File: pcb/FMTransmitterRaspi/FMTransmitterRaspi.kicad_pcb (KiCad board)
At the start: 2 copper layers, 56.6 x 52.3 mm, 35 parts, among them J1 Antenna/External Power, J2 GPIO, J3 GPIO, J4 USB-C Power, J5 Line In/Out, J6 Line In/Out 2, U1 QN8072, U2 PCM5102A, U3 ME6211C33M5, Y1 24MHz, Y2 12MHz

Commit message: corrected wrong symbol of qn8027, too wide board shape
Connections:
- U1 pad 10: /GPIO3/SCL1 -> Net-(U1-ALI)
- U1 pad 6: Net-(U1-ALI) -> /GPIO3/SCL1
- U1 pad 7: Net-(U1-ARI) -> /GPIO2/SDA1
- U1 pad 9: /GPIO2/SDA1 -> Net-(U1-ARI)
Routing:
- net /GPIO3/SCL1: track 35.6 -> 44.0 mm, vias 0 -> 2
- net Net-(U1-ALI): track 18.2 -> 10.4 mm
- net /GPIO2/SDA1: track 36.9 -> 42.9 mm, vias 0 -> 2
- net Net-(U1-ARI): track 8.46 -> 7.22 mm
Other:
- board size 56.6 x 52.3 mm -> 56.4 x 52.3 mm
- board text added: "Raspi Audio DAC FM Transmitter Bernd Strobel 09/2026 Rev. 1"
- board text removed: "Raspi Audio DAC FM Transmitter Bernd Strobel 09/2026"

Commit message: pcb beautified
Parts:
- C14, C9: value 2u2 -> 470n
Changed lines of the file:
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@@
 		(tags "C Rect series Radial pin pitch 7.50mm length 9mm width 2.7mm Capacitor")
 		(property "Reference" "C18"
-			(at 6.544 2.54 0)
+			(at 7.56 2.54 0)
 			(layer "F.SilkS")
 			(effects
@@
 		)
 		(property "Value" "2.2n"
-			(at 1.464 2.54 0)
+			(at 4.004 2.54 0)
 			(layer "F.SilkS")
 			(effects
@@
 		(at 156.308 130.988 -90)
 		(property "Reference" "J5"
-			(at 5.842 10.588 0)
+			(at -5.842 10.842 0)
 			(unlocked yes)
 			(layer "F.SilkS")
@@
 		)
 		(property "Value" "Line In/Out"
-			(at 5.842 4.746 0)
+			(at -5.842 5 0)
 			(unlocked yes)
 			(layer "F.SilkS")
@@
 		(tags "C Rect series Radial pin pitch 5.00mm length 7.2mm width 6.0mm Capacitor R82")
 		(property "Reference" "C14"
-			(at 7.032 -1.778 180)
+			(at -2.112 -1.524 180)
 			(layer "F.SilkS")
 			(effects
@@
 			)
 		)
-		(property "Value" "2u2"
-			(at 7.032 1.524 180)
+		(property "Value" "470n"
+			(at -2.112 2.032 180)
 			(layer "F.SilkS")
 			(effects
@@
 		(tags "C Rect series Radial pin pitch 5.00mm length 7.2mm width 6.0mm Capacitor R82")
 		(property "Reference" "C9"
-			(at 7.072 -1.016 180)
+			(at 8.596 0.762 180)
 			(layer "F.SilkS")
 			(effects
@@
 			)
 		)
-		(property "Value" "2u2"
-			(at 7.072 1.778 180)
+		(property "Value" "470n"
+			(at 7.072 0.762 180)
 			(layer "F.SilkS")
 			(effects
@@
 	)
 	(segment
-		(start 115.374 105.468)
-		(end 114.224 104.318)
+		(start 135.564 114.983807)
+		(end 135.564 111.921882)
 		(width 0.2)
 		(layer "F.Cu")
-		(net "/GPIO2{slash}SDA1")
+		(net "/GPIO3{slash}SCL1")
 	)
 	(segment
-		(start 117.592778 105.468)
-		(end 117.592778 106.033685)
+		(start 101.778 106.858)
+		(end 103.168 108.248)
 		(width 0.2)
 		(layer "F.Cu")
-		(net "/GPIO2{slash}SDA1")
+		(net "/GPIO3{slash}SCL1")
 	)
 	(segment
-		(start 135.164 113.849094)
-		(end 135.164 112.087568)
+		(start 114.224 106.858)
+		(end 114.789685 106.858)
 		(width 0.2)
 		(layer "F.Cu")
-		(net "/GPIO2{slash}SDA1")
+		(net "/GPIO3{slash}SCL1")
 	)
 	(segment
-		(start 103.168 105.708)
-		(end 112.834 105.708)
+		(start 114.789685 106.858)
+		(end 115.939685 108.008)
 		(width 0.2)
 		(layer "F.Cu")
-		(net "/GPIO2{slash}SDA1")
+		(net "/GPIO3{slash}SCL1")
 	)
 	(segment
-		(start 112.834 105.708)
-		(end 114.224 104.318)
+		(start 135.052754 115.495053)
+		(end 135.564 114.983807)
 		(width 0.2)
 		(layer "F.Cu")
-		(net "/GPIO2{slash}SDA1")
+		(net "/GPIO3{slash}SCL1")
 	)
 	(segment
-		(start 124.044093 112.485)
-		(end 130.731411 112.485)
+		(start 124.213407 113.22)
+		(end 129.911243 113.22)
 		(width 0.2)
 		(layer "F.Cu")
-		(net "/GPIO2{slash}SDA1")
+		(net "/GPIO3{slash}SCL1")
 	)
 	(segment
-		(start 135.164 112.087568)
-		(end 134.514432 111.438)
+		(start 129.911243 113.22)
+		(end 129.934728 113.243485)
 		(width 0.2)
 		(layer "F.Cu")
-		(net "/GPIO2{slash}SDA1")
+		(net "/GPIO3{slash}SCL1")
 	)
 	(segment
-		(start 134.412547 114.600547)
-		(end 135.164 113.849094)
+		(start 119.001407 108.008)
+		(end 124.213407 113.22)
 		(width 0.2)
 		(layer "F.Cu")
-		(net "/GPIO2{slash}SDA1")
+		(net "/GPIO3{slash}SCL1")
 	)
 	(segment
-		(start 134.514432 111.438)
-		(end 133.714 111.438)
+		(start 135.564 111.921882)
+		(end 134.580118 110.938)
 		(width 0.2)
 		(layer "F.Cu")
-		(net "/GPIO2{slash}SDA1")
+		(net "/GPIO3{slash}SCL1")
 	)
 	(segment
-		(start 117.592778 106.033685)
-		(end 124.044093 112.485)
+		(start 112.834 108.248)
+		(end 114.224 106.858)
 		(width 0.2)
 		(layer "F.Cu")
-		(net "/GPIO2{slash}SDA1")
+		(net "/GPIO3{slash}SCL1")
 	)
 	(segment
-		(start 101.778 104.318)
-		(end 103.168 105.708)
+		(start 115.939685 108.008)
+		(end 119.001407 108.008)
 		(width 0.2)
 		(layer "F.Cu")
-		(net "/GPIO2{slash}SDA1")
+		(net "/GPIO3{slash}SCL1")
 	)
 	(segment
-		(start 117.592778 105.468)
-		(end 115.374 105.468)
+		(start 103.168 108.248)
+		(end 112.834 108.248)
 		(width 0.2)
 		(layer "F.Cu")
-		(net "/GPIO2{slash}SDA1")
+		(net "/GPIO3{slash}SCL1")
+	)
+	(segment
+		(start 134.580118 110.938)
+		(end 133.714 110.938)
+		(width 0.2)
+		(layer "F.Cu")
+		(net "/GPIO3{slash}SCL1")
 	)
 	(via
-		(at 130.731411 112.485)
+		(at 129.934728 113.243485)
 		(size 0.9)
 		(drill 0.6)
 		(layers "F.Cu" "B.Cu")
-		(net "/GPIO2{slash}SDA1")
+		(net "/GPIO3{slash}SCL1")
 	)
 	(via
-		(at 134.412547 114.600547)
+		(at 135.052754 115.495053)
 		(size 0.9)
 		(drill 0.6)
 		(layers "F.Cu" "B.Cu")
-		(net "/GPIO2{slash}SDA1")
+		(net "/GPIO3{slash}SCL1")
 	)
 	(segment
-		(start 130.731411 112.485)
-		(end 132.846958 114.600547)
+		(start 129.934728 113.243485)
+		(end 132.186296 115.495053)
 		(width 0.2)
 		(layer "B.Cu")
-		(net "/GPIO2{slash}SDA1")
+		(net "/GPIO3{slash}SCL1")
 	)
 	(segment
-		(start 132.846958 114.600547)
-		(end 134.412547 114.600547)
+		(start 132.186296 115.495053)
+		(end 135.052754 115.495053)
 		(width 0.2)
 		(layer "B.Cu")
-		(net "/GPIO2{slash}SDA1")
-	)
-	(segment
-		(start 135.564 114.983807)
-		(end 135.564 111.921882)
-		(width 0.2)
-		(layer "F.Cu")
 		(net "/GPIO3{slash}SCL1")
 	)
 	(segment
-		(start 101.778 106.858)
-		(end 103.168 108.248)
+		(start 115.374 105.468)
+		(end 114.224 104.318)
 		(width 0.2)
 		(layer "F.Cu")
-		(net "/GPIO3{slash}SCL1")
+		(net "/GPIO2{slash}SDA1")
 	)
 	(segment
-		(start 114.224 106.858)
-		(end 114.789685 106.858)
+		(start 117.592778 105.468)
+		(end 117.592778 106.033685)
 		(width 0.2)
 		(layer "F.Cu")
-		(net "/GPIO3{slash}SCL1")
+		(net "/GPIO2{slash}SDA1")
 	)
 	(segment
-		(start 114.789685 106.858)
-		(end 115.939685 108.008)
+		(start 135.164 113.849094)
+		(end 135.164 112.087568)
 		(width 0.2)
 		(layer "F.Cu")
-		(net "/GPIO3{slash}SCL1")
+		(net "/GPIO2{slash}SDA1")
 	)
 	(segment
-		(start 135.052754 115.495053)
-		(end 135.564 114.983807)
+		(start 103.168 105.708)
+		(end 112.834 105.708)
 		(width 0.2)
 		(layer "F.Cu")
-		(net "/GPIO3{slash}SCL1")
+		(net "/GPIO2{slash}SDA1")
 	)
 	(segment
-		(start 124.213407 113.22)
-		(end 129.911243 113.22)
+		(start 112.834 105.708)
+		(end 114.224 104.318)
 		(width 0.2)
 		(layer "F.Cu")
-		(net "/GPIO3{slash}SCL1")
+		(net "/GPIO2{slash}SDA1")
 	)
 	(segment
-		(start 129.911243 113.22)
-		(end 129.934728 113.243485)
+		(start 124.044093 112.485)
+		(end 130.731411 112.485)
 		(width 0.2)
 		(layer "F.Cu")
-		(net "/GPIO3{slash}SCL1")
+		(net "/GPIO2{slash}SDA1")
 	)
 	(segment
-		(start 119.001407 108.008)
-		(end 124.213407 113.22)
+		(start 135.164 112.087568)
+		(end 134.514432 111.438)
 		(width 0.2)
 		(layer "F.Cu")
-		(net "/GPIO3{slash}SCL1")
+		(net "/GPIO2{slash}SDA1")
 	)
 	(segment
-		(start 135.564 111.921882)
-		(end 134.580118 110.938)
+		(start 134.412547 114.600547)
+		(end 135.164 113.849094)
 		(width 0.2)
 		(layer "F.Cu")
-		(net "/GPIO3{slash}SCL1")
+		(net "/GPIO2{slash}SDA1")
 	)
 	(segment
-		(start 112.834 108.248)
-		(end 114.224 106.858)
+		(start 134.514432 111.438)
+		(end 133.714 111.438)
 		(width 0.2)
 		(layer "F.Cu")
-		(net "/GPIO3{slash}SCL1")
+		(net "/GPIO2{slash}SDA1")
 	)
 	(segment
-		(start 115.939685 108.008)
-		(end 119.001407 108.008)
+		(start 117.592778 106.033685)
+		(end 124.044093 112.485)
 		(width 0.2)
 		(layer "F.Cu")
-		(net "/GPIO3{slash}SCL1")
+		(net "/GPIO2{slash}SDA1")
 	)
 	(segment
-		(start 103.168 108.248)
-		(end 112.834 108.248)
+		(start 101.778 104.318)
+		(end 103.168 105.708)
 		(width 0.2)
 		(layer "F.Cu")
-		(net "/GPIO3{slash}SCL1")
+		(net "/GPIO2{slash}SDA1")
 	)
 	(segment
-		(start 134.580118 110.938)
-		(end 133.714 110.938)
+		(start 117.592778 105.468)
+		(end 115.374 105.468)
 		(width 0.2)
 		(layer "F.Cu")
-		(net "/GPIO3{slash}SCL1")
+		(net "/GPIO2{slash}SDA1")
 	)
 	(via
-		(at 129.934728 113.243485)
+		(at 130.731411 112.485)
 		(size 0.9)
 		(drill 0.6)
 		(layers "F.Cu" "B.Cu")
-		(net "/GPIO3{slash}SCL1")
+		(net "/GPIO2{slash}SDA1")
 	)
 	(via
-		(at 135.052754 115.495053)
+		(at 134.412547 114.600547)
 		(size 0.9)
 		(drill 0.6)
 		(layers "F.Cu" "B.Cu")
-		(net "/GPIO3{slash}SCL1")
+		(net "/GPIO2{slash}SDA1")
 	)
 	(segment
-		(start 129.934728 113.243485)
-		(end 132.186296 115.495053)
+		(start 130.731411 112.485)
+		(end 132.846958 114.600547)
 		(width 0.2)
 		(layer "B.Cu")
-		(net "/GPIO3{slash}SCL1")
+		(net "/GPIO2{slash}SDA1")
 	)
 	(segment
-		(start 132.186296 115.495053)
-		(end 135.052754 115.495053)
+		(start 132.846958 114.600547)
+		(end 134.412547 114.600547)
 		(width 0.2)
 		(layer "B.Cu")
-		(net "/GPIO3{slash}SCL1")
+		(net "/GPIO2{slash}SDA1")
 	)
 	(segment

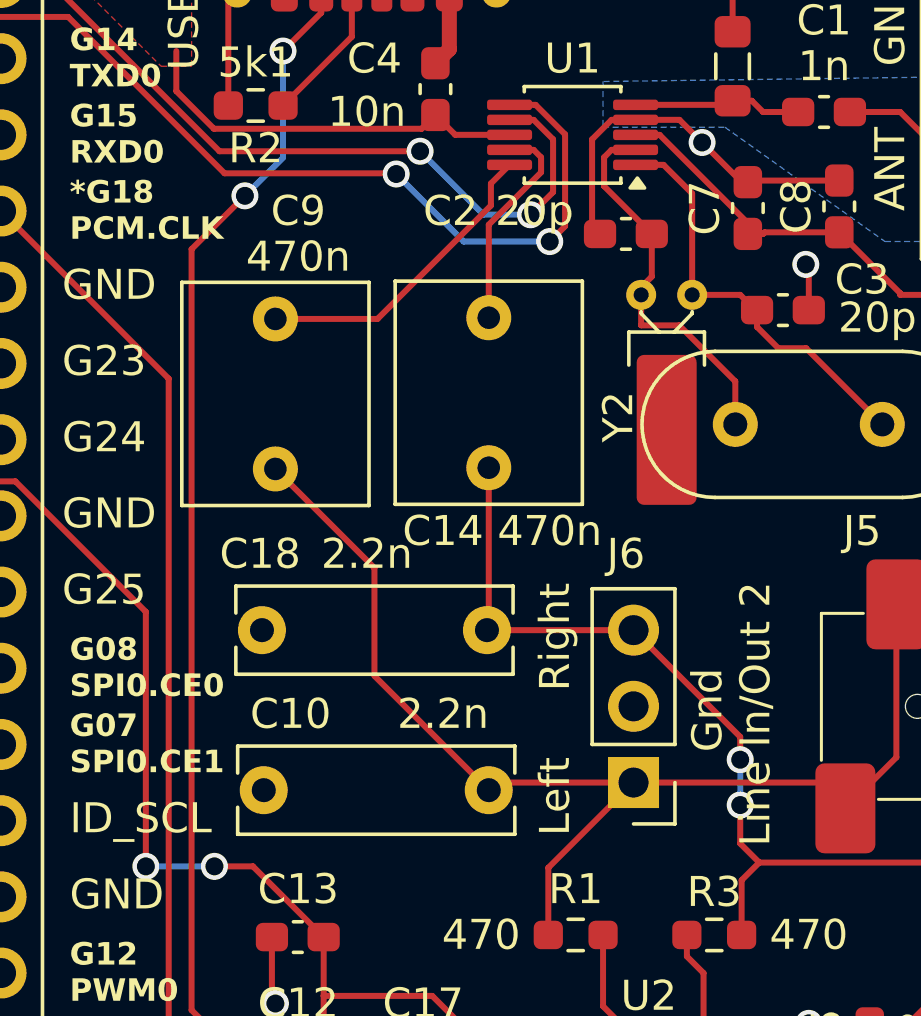
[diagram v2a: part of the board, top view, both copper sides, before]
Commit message: added voltage divider between pcm5102 and qn8027
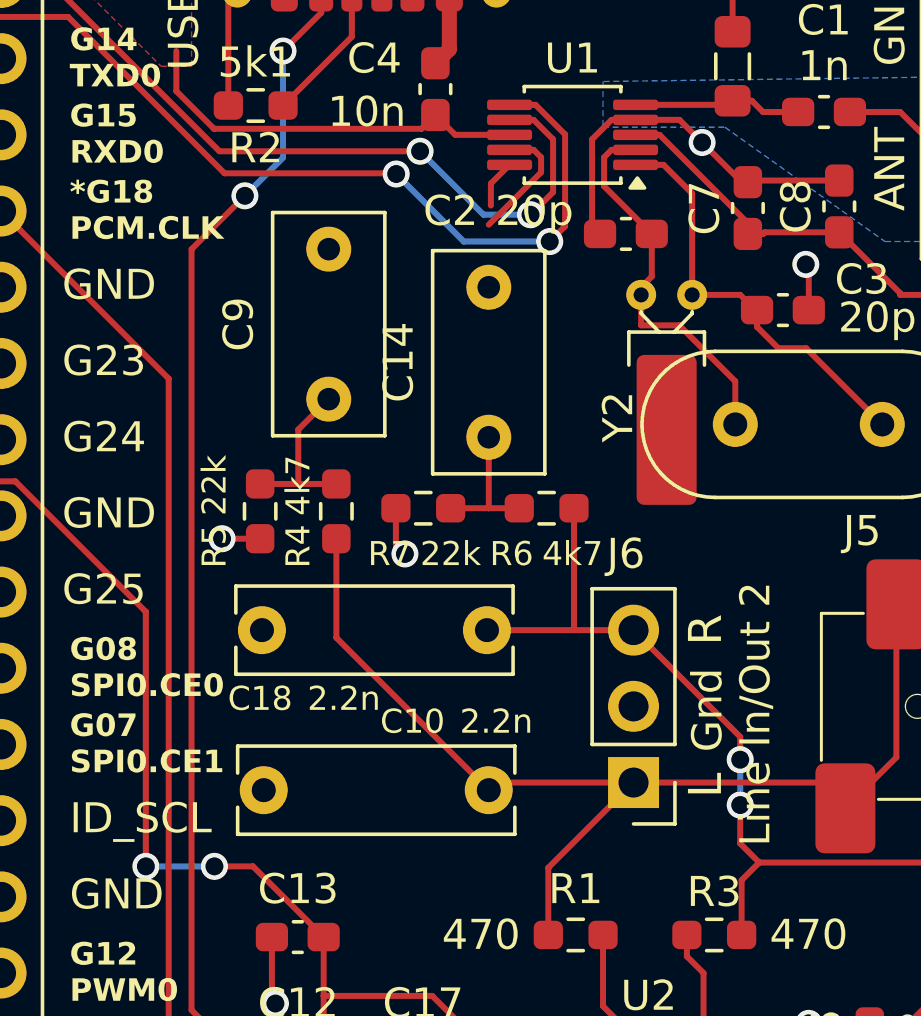
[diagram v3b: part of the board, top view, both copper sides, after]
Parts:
- added R4: 4k7, Resistor_SMD:R_0603_1608Metric_Pad0.98x0.95mm_HandSolder, F.Cu at (127.9, 124.5)
- added R5: 22k, Resistor_SMD:R_0603_1608Metric_Pad0.98x0.95mm_HandSolder, F.Cu at (125.4, 124.5)
- added R6: 4k7, Resistor_SMD:R_0603_1608Metric_Pad0.98x0.95mm_HandSolder, F.Cu at (134.9, 124.4)
- added R7: 22k, Resistor_SMD:R_0603_1608Metric_Pad0.98x0.95mm_HandSolder, F.Cu at (130.8, 124.4)
- C14, C9: footprint Capacitor_THT:C_Rect_L7.2mm_W6.0mm_P5.00mm -> Capacitor_THT:C_Rect_L7.2mm_W3.5mm_P5.00mm
- moved C9 2.93 mm to (127.7, 120.7)
- moved C14 1.02 mm to (133.0, 122.0)
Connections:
- C14 pad 1: Net-(J6-Pin_3) -> Net-(C14-Pad1)
- C9 pad 1: Net-(J6-Pin_1) -> Net-(C9-Pad1)
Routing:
- net Net-(U1-ALI): track 10.4 -> 1.62 mm
- net Net-(C9-Pad1): track 0.00 -> 5.79 mm
- net Net-(C14-Pad1): track 0.00 -> 4.65 mm
- net GND: track 78.8 -> 82.4 mm, vias 13 -> 15
- net Net-(J6-Pin_1): track 39.8 -> 36.6 mm
- net Net-(U1-ARI): track 7.22 -> 4.12 mm
- net Net-(J6-Pin_3): track 32.1 -> 30.8 mm
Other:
- board text added: "L"
- board text added: "R"
- board text removed: "Left"
- board text removed: "Right"

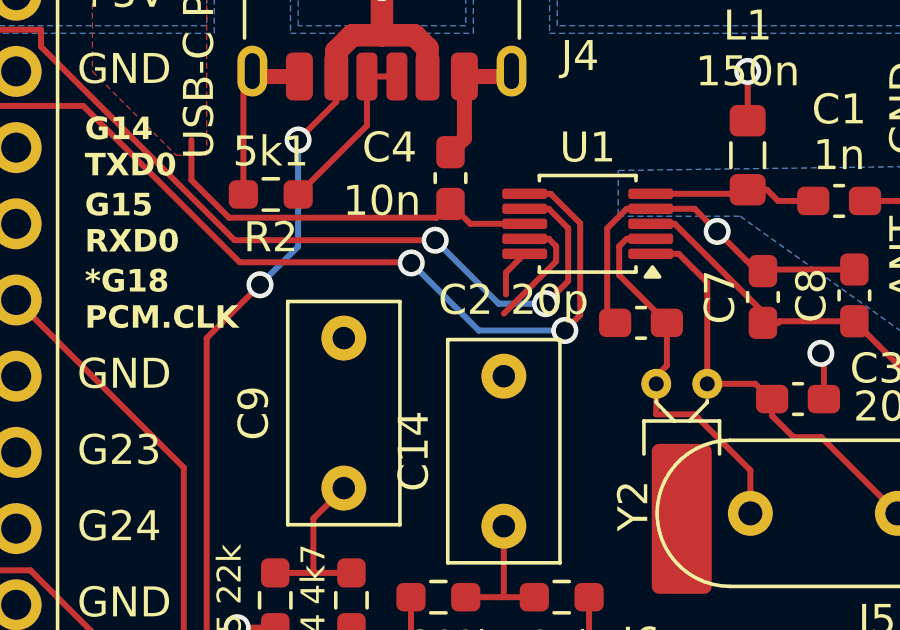
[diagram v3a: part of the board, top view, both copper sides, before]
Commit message: forgot to route 2 connections...
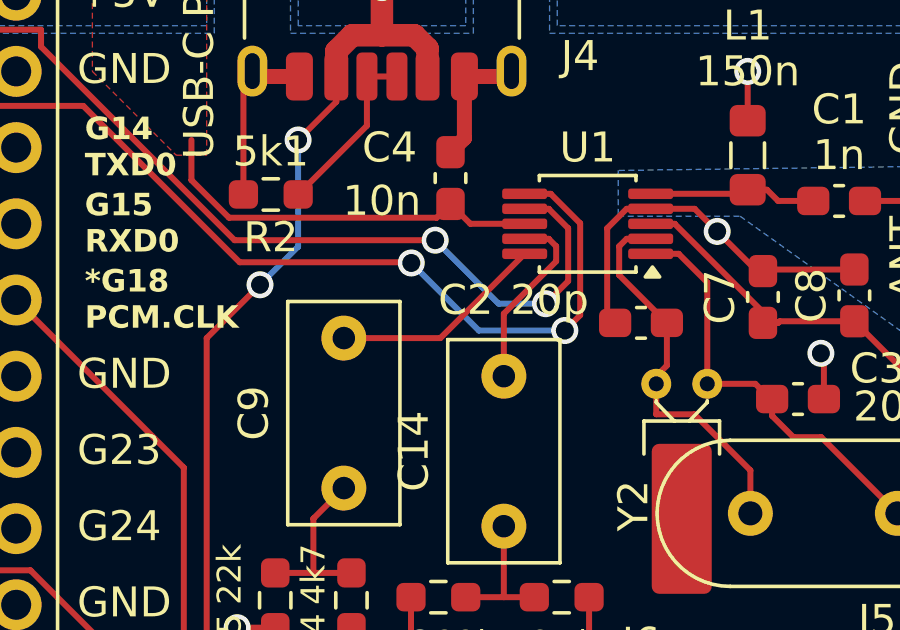
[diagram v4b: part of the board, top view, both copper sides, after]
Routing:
- net Net-(U1-ALI): track 1.62 -> 7.19 mm
- net Net-(U1-ARI): track 4.12 -> 6.21 mm
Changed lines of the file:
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@@
+	)
+	(segment
+		(start 134.764 113.188432)
+		(end 133.02 114.932432)
+		(width 0.2)
+		(layer "F.Cu")
+		(net "Net-(U1-ARI)")
 	)
 	(segment
 		(start 133.02 114.932432)
-		(end 134.764 113.188432)
+		(end 133.02 117.018)
 		(width 0.2)
 		(layer "F.Cu")
@@
 	)
 	(segment
-		(start 133.091373 113.560627)
+		(start 127.686 115.748)
+		(end 130.904 115.748)
+		(width 0.2)
+		(layer "F.Cu")
+		(net "Net-(U1-ALI)")
+	)
+	(segment
+		(start 130.904 115.748)
 		(end 133.714 112.938)
 		(width 0.2)
 		(layer "F.Cu")
-		(net "Net-(U1-ALI)")
-	)
-	(segment
-		(start 133.091373 114.295373)
-		(end 133.091373 113.560627)
-		(width 0.2)
-		(layer "F.Cu")
